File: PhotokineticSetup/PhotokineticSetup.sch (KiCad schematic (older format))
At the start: 25 parts, among them J1 Conn_01x02, J2 Serial, J3 LEDs, J4 Switches, J5 Outputs, J6 Inputs, J7 Conn_01x20, J8 Conn_01x20, U1 MAX232, U2 ILD615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

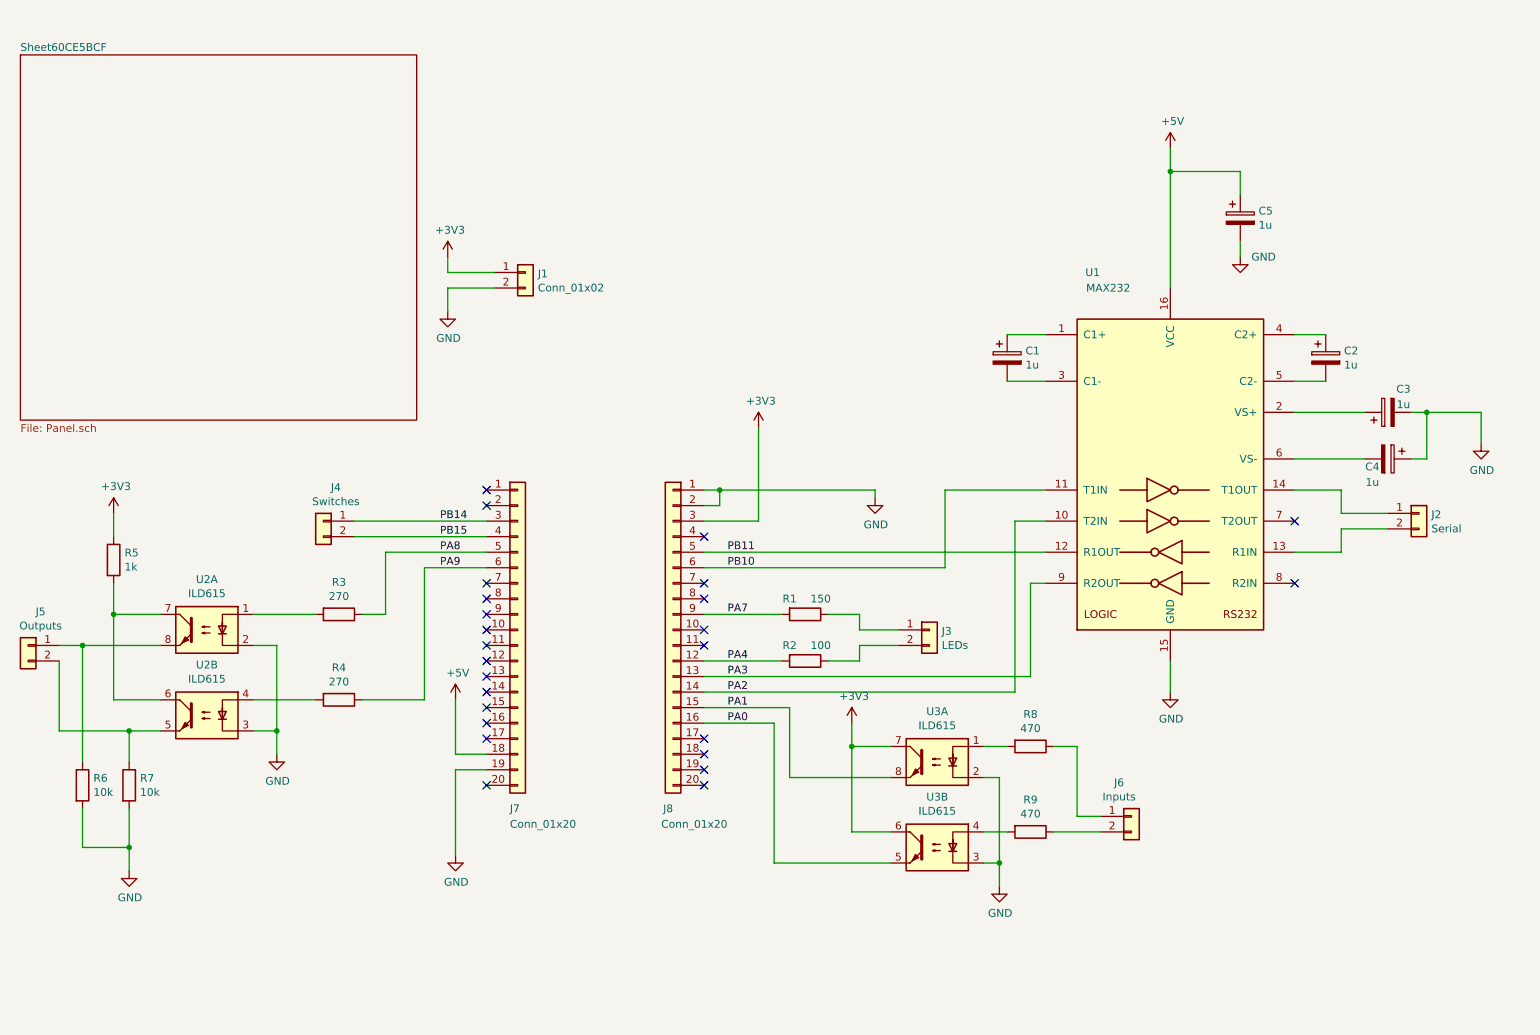
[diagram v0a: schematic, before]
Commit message: Clearer optocouplers outputs and stronger input
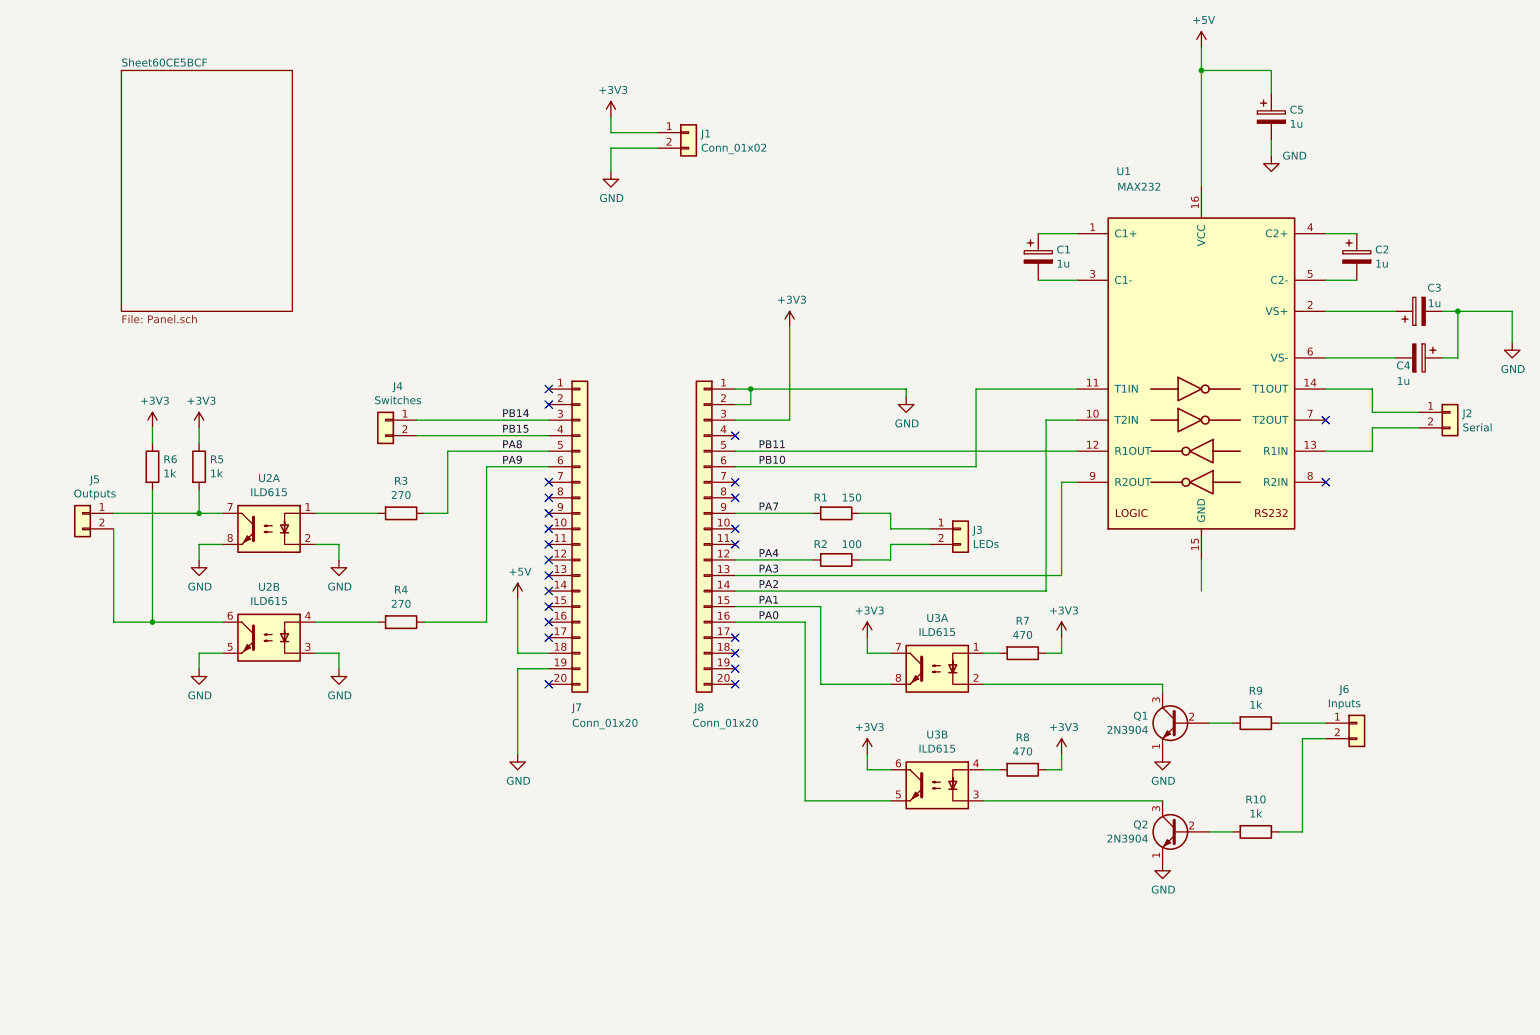
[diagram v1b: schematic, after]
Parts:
- removed R7: 10k, Resistor_THT:R_Axial_DIN0204_L3.6mm_D1.6mm_P7.62mm_Horizontal, symbol Device:R
- added Q1, Q2: 2N3904, Package_TO_SOT_THT:TO-92_Inline, symbol Transistor_BJT:2N3904
- added R10, R9: 1k, Resistor_THT:R_Axial_DIN0204_L3.6mm_D1.6mm_P7.62mm_Horizontal, symbol Device:R
- R6: value 10k -> 1k
- renumbered R8 to R7, R9 to R8
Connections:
- net +3V3: now also R6.1, R7.1, R8.1
- net GND: now also U2.5, U2.8, Q1.1 (E), Q2.1 (E); no longer R6.2, U1.15 (GND), U3.2, U3.3
- net at J5.2 (Pin_2): now also R6.2, U2.6; no longer U2.5
- net at R5.2, U2.7: now also J5.1 (Pin_1); no longer U2.6
- net at J6.1 (Pin_1): now also R9.1; no longer R7.1
- net at J6.2 (Pin_2): now also R10.1; no longer R8.1
- new net: Q1.3 (C), U3.2
- new net: Q2.3 (C), U3.3
- new net: Q1.2 (B), R9.2
- new net: Q2.2 (B), R10.2
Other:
- moved on the sheet: C1, C2, C3, C4, C5, J1, J2, J3, J4, J5, J6, J7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

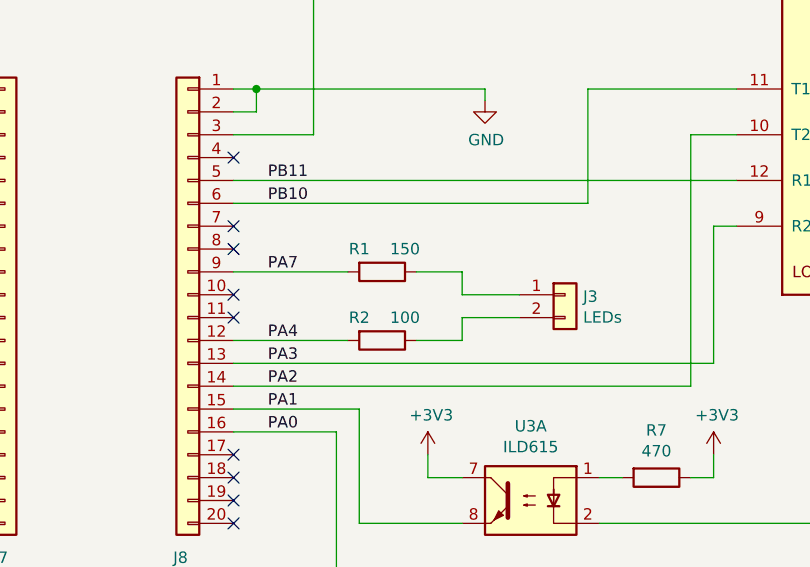
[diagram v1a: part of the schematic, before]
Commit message: LED resistors calculated according to forward voltage
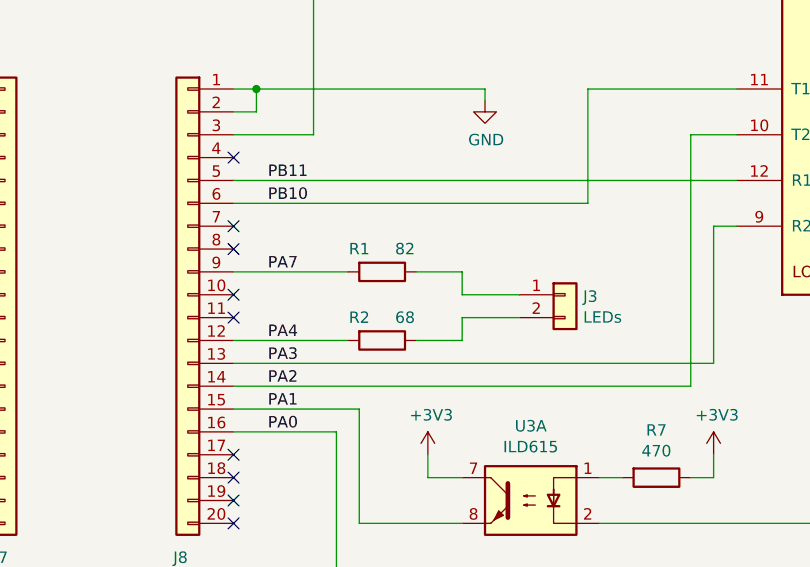
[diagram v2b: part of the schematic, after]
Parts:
- R1: value 150 -> 82
- R2: value 100 -> 68
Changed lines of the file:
@@
 P 5900 3850
 F 0 "R1" V 5800 3750 50  0000 C CNN
-F 1 "150" V 5800 3950 50  0000 C CNN
+F 1 "82" V 5800 3950 50  0000 C CNN
 F 2 "Resistor_THT:R_Axial_DIN0204_L3.6mm_D1.6mm_P7.62mm_Horizontal" V 5830 3850 50  0001 C CNN
 F 3 "~" H 5900 3850 50  0001 C CNN
@@
 P 5900 4150
 F 0 "R2" V 5800 4050 50  0000 C CNN
-F 1 "100" V 5800 4250 50  0000 C CNN
+F 1 "68" V 5800 4250 50  0000 C CNN
 F 2 "Resistor_THT:R_Axial_DIN0204_L3.6mm_D1.6mm_P7.62mm_Horizontal" V 5830 4150 50  0001 C CNN
 F 3 "~" H 5900 4150 50  0001 C CNN
